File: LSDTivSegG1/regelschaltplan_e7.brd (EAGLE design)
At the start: 160 x 100 mm, 90 parts, among them IC1 LF33AB, IC3 MAX232, IC4 MEGA32-P, Q2 BS170, Q3 BS170, Q4 BS170, Q5 BS170, Q6 BS170, Q7 BS170, Q8 BS170

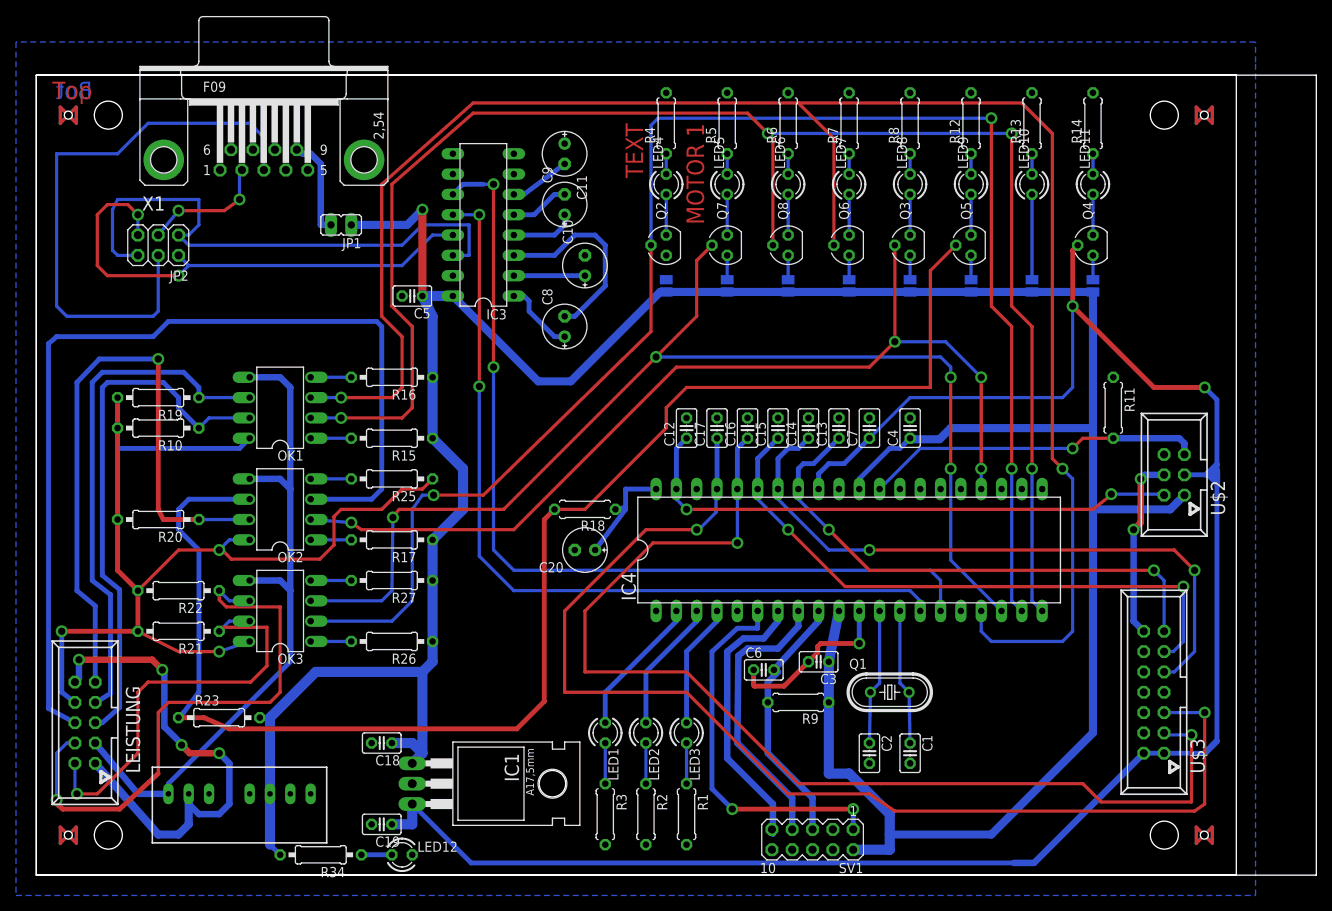
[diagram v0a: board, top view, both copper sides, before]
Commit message: added Text on Layers for identification
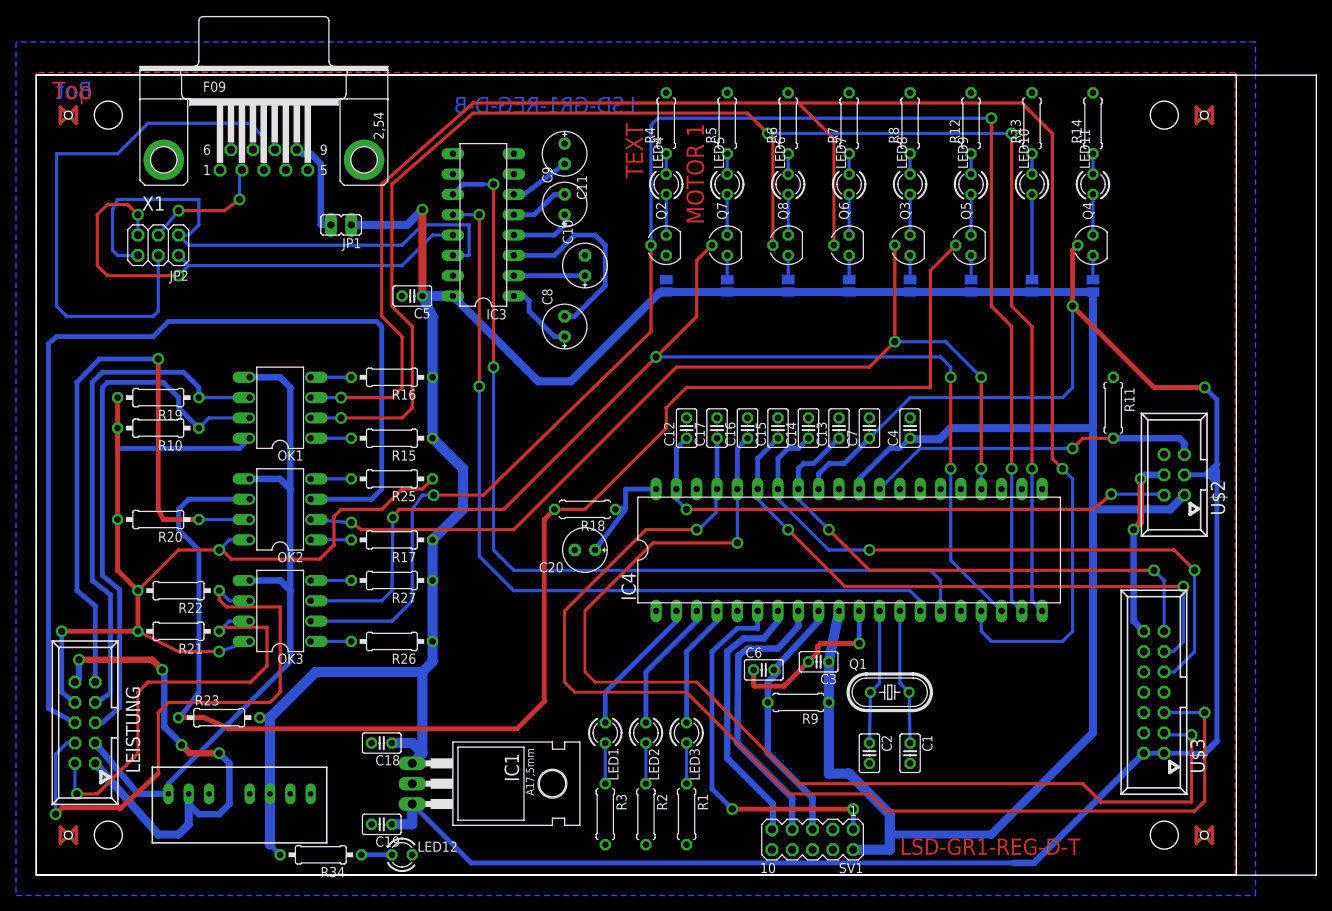
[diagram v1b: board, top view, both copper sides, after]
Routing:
- net N$49: track 71.9 -> 73.6 mm
- net ACCEL_Y: track 146.2 -> 145.6 mm
- added copper zone on layer 1, net GND
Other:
- board text added: "LSD-GR1-REG-D-B"
- board text added: "LSD-GR1-REG-D-BSTOP"
- board text added: "LSD-GR1-REG-D-T"
- board text added: "LSD-GR1-REG-D-TSTOP"
